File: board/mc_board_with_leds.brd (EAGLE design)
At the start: 131 x 76.6 mm, 30 parts, among them IC2 MEGA8-P, Q2 16MHz

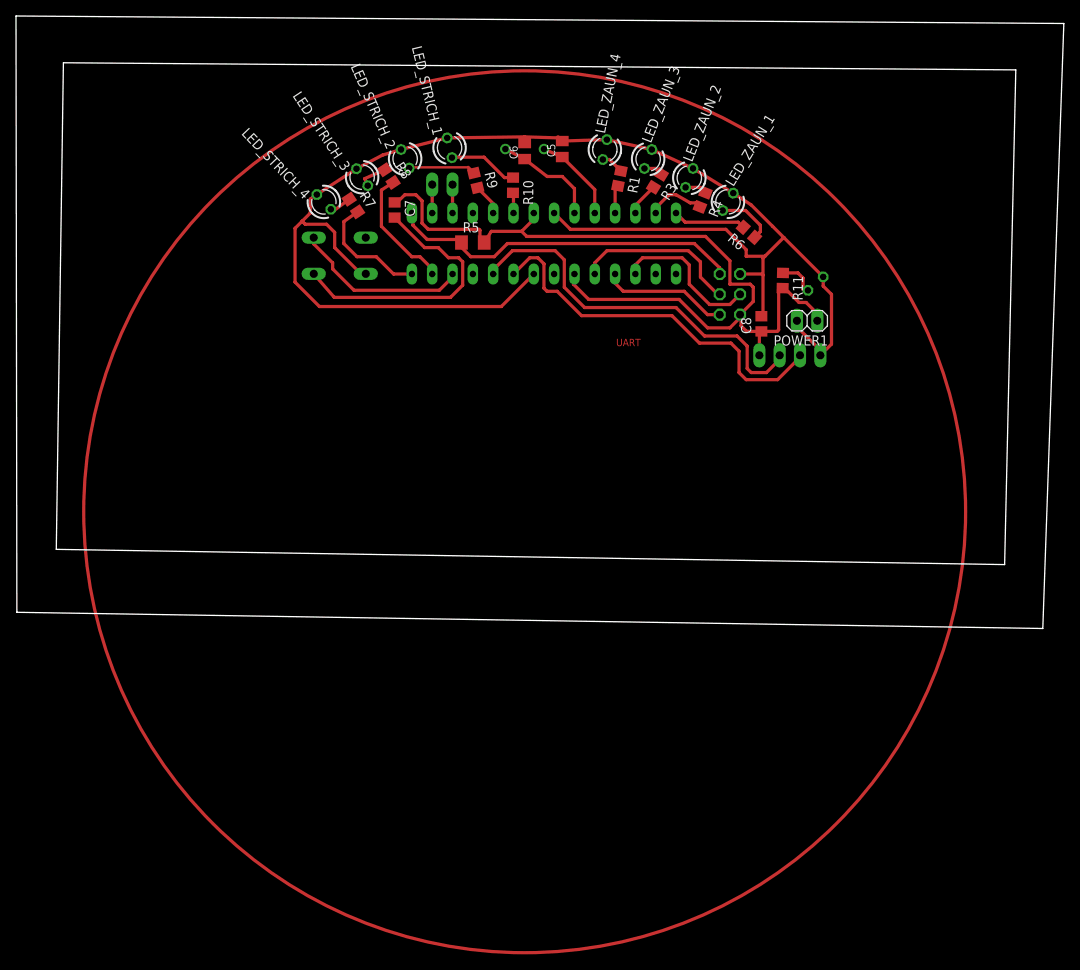
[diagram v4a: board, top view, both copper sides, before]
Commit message: added step up converter to schematic
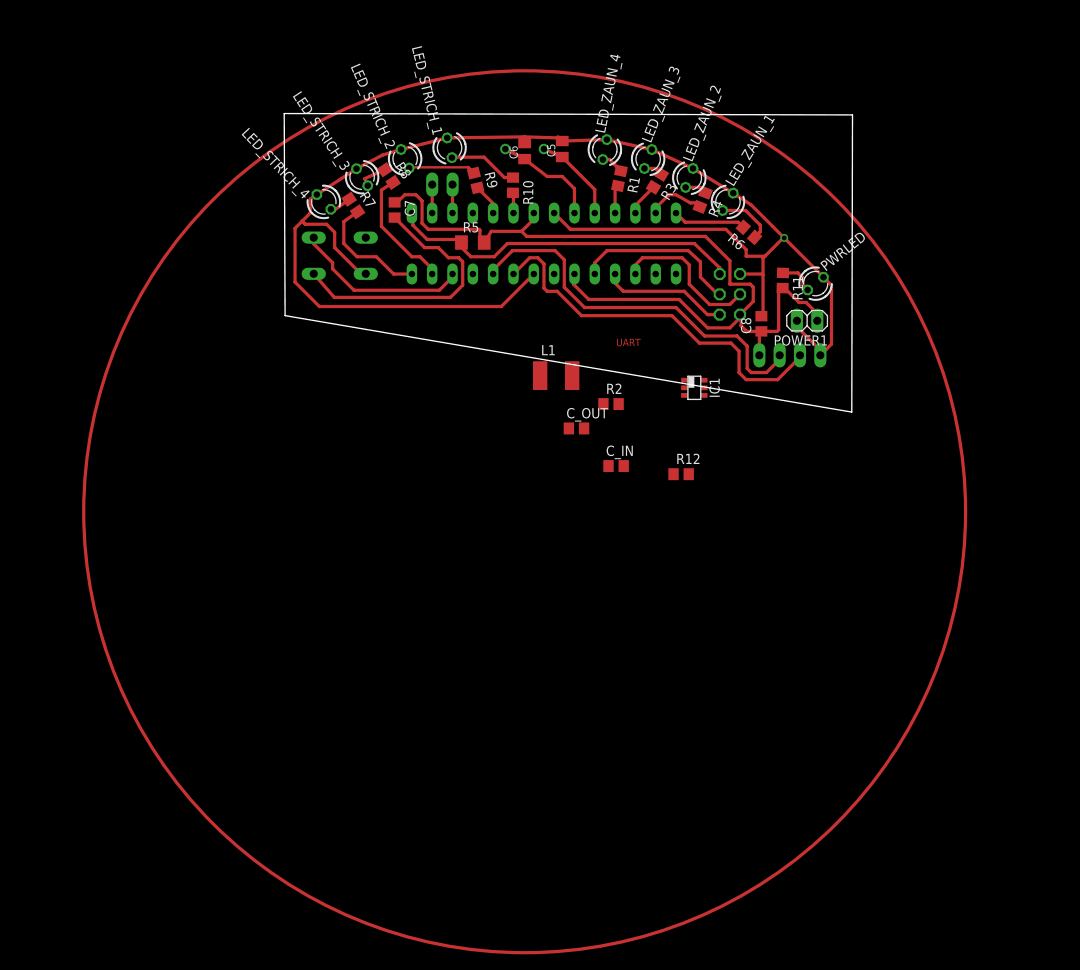
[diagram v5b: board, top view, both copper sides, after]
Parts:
- added C_IN, C_OUT: (no value), rcl-2:C0805
- added IC1: TPS61070DDC, texas:TSOT23-6_DDC
- added L1: (no value), rcl:L4532P
- added R12, R2: (no value), resistor:R0805
- flipped PWRLED to the top, turned to 38.6 degrees
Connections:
- new net N$5: IC1.1, L1.2
- new net N$6: IC1.4, R12.1, R2.2
- new net V_IN: C_IN.1, IC1.3, IC1.6, L1.1, POWER1.1
- net +5V: now also C_OUT.1, IC1.5, R2.1; no longer POWER1.1
- net GND: now also C_IN.2, C_OUT.2, IC1.2, R12.2
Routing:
- net +5V: track 109.2 -> 108.3 mm
- net GND: vias 0 -> 1
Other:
- board size 131 x 76.6 mm -> 71 x 37.3 mm
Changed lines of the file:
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@@
 <layer number="220" name="220bmp" color="21" fill="1" visible="no" active="no"/>
 <layer number="221" name="221bmp" color="22" fill="1" visible="no" active="no"/>
-<layer number="222" name="222bmp" color="23" fill="1" visible="no" active="no"/>
+<layer number="222" name="imagesize" color="23" fill="1" visible="yes" active="yes"/>
 <layer number="223" name="223bmp" color="24" fill="1" visible="no" active="no"/>
 <layer number="224" name="224bmp" color="25" fill="1" visible="no" active="no"/>
@@
 <board>
 <plain>
-<wire x1="-3.302" y1="-4.699" x2="115.24" y2="-6.604" width="0" layer="20"/>
-<wire x1="115.24" y1="-6.604" x2="116.637" y2="55.235" width="0" layer="20"/>
-<wire x1="116.637" y1="55.235" x2="-2.413" y2="56.124" width="0" layer="20"/>
-<wire x1="-2.413" y1="56.124" x2="-3.302" y2="-4.699" width="0" layer="20"/>
 <text x="66.675" y="20.701" size="0.9144" layer="1" font="vector" ratio="28">UART</text>
-<wire x1="-8.229528125" y1="-12.56735625" x2="-8.338403125" y2="61.970115625" width="0" layer="20"/>
-<wire x1="-8.338403125" y1="61.970115625" x2="122.64075" y2="61.033575" width="0" layer="20"/>
-<wire x1="122.64075" y1="61.033575" x2="120.011409375" y2="-14.59155" width="0" layer="20"/>
-<wire x1="120.011409375" y1="-14.59155" x2="-8.229528125" y2="-12.56735625" width="0" layer="20"/>
+<wire x1="25.298471875" y1="24.51664375" x2="25.189596875" y2="49.778115625" width="0" layer="20"/>
+<wire x1="25.189596875" y1="49.778115625" x2="96.22475" y2="49.603575" width="0" layer="20"/>
+<wire x1="96.22475" y1="49.603575" x2="96.135409375" y2="12.45945" width="0" layer="20"/>
+<wire x1="96.135409375" y1="12.45945" x2="25.298471875" y2="24.51664375" width="0" layer="20"/>
 <circle x="55.245" y="0" radius="55.118" width="0.4064" layer="1"/>
 </plain>
@@
 <element name="R10" library="resistor" package="R0805" value="470" x="53.788540625" y="40.819409375" rot="R269.6"/>
 <element name="R11" library="resistor" package="R0805" value="470" x="87.511846875" y="28.906165625" rot="R268.6"/>
-<element name="PWRLED" library="led" package="LED3MM" value="" x="91.60673125" y="28.5177875" rot="MR138.6"/>
+<element name="PWRLED" library="led" package="LED3MM" value="" x="91.60673125" y="28.5177875" rot="R38.6"/>
 <element name="Q2" library="crystal" package="HC49/S" value="16MHz" x="55.245" y="45.339" rot="MR0">
 <attribute name="MPN" value="" x="65.913" y="71.755" size="1.778" layer="28" rot="MR0" display="off"/>
@@
 <element name="HX1" library="pinhead" package="1X04" value="JP1" x="88.392" y="19.558" rot="MR0"/>
 <element name="UART1" library="pinhead" package="1X02" value="JP2" x="44.958" y="40.894" rot="MR180"/>
+<element name="IC1" library="texas" package="TSOT23-6_DDC" value="TPS61070DDC" x="76.454" y="15.494" rot="R270">
+<attribute name="MPN" value="TPS61070DDCR" x="76.454" y="15.494" size="1.778" layer="27" rot="R270" display="off"/>
+<attribute name="OC_NEWARK" value="64M3125" x="76.454" y="15.494" size="1.778" layer="27" rot="R270" display="off"/>
+<attribute name="MF" value="" x="76.454" y="15.494" size="1.778" layer="27" rot="R270" display="off"/>
+<attribute name="OC_FARNELL" value="1461062" x="76.454" y="15.494" size="1.778" layer="27" rot="R270" display="off"/>
+</element>
+<element name="L1" library="rcl" package="L4532P" value="" x="59.182" y="17.018"/>
+<element name="R2" library="resistor" package="R0805" value="" x="66.04" y="13.462"/>
+<element name="R12" library="resistor" package="R0805" value="" x="74.803" y="4.699"/>
+<element name="C_IN" library="rcl-2" package="C0805" value="" x="66.675" y="5.715"/>
+<element name="C_OUT" library="rcl-2" package="C0805" value="" x="61.722" y="10.414"/>
 </elements>
 <signals>
@@
 <wire x1="80.391" y1="35.306" x2="60.96" y2="35.306" width="0.4064" layer="1"/>
 <wire x1="60.96" y1="35.306" x2="58.928" y2="37.338" width="0.4064" layer="1"/>
-<wire x1="92.559375" y1="29.357653125" x2="87.693203125" y2="34.2261125" width="0.4064" layer="1"/>
 <wire x1="87.693203125" y1="34.2261125" x2="86.233" y2="35.687" width="0.4064" layer="1"/>
 <wire x1="81.31878125" y1="39.828921875" x2="83.566" y2="38.354" width="0.4064" layer="1"/>
@@
 <wire x1="87.5661125" y1="34.2261125" x2="87.693203125" y2="34.2261125" width="0.4064" layer="1"/>
 <wire x1="92.202" y1="19.558" x2="93.599" y2="20.955" width="0.4064" layer="1"/>
-<wire x1="93.599" y1="20.955" x2="93.599" y2="27.178" width="0.4064" layer="1"/>
-<wire x1="93.599" y1="27.178" x2="92.559375" y2="28.217625" width="0.4064" layer="1"/>
-<wire x1="92.559375" y1="28.217625" x2="92.559375" y2="29.357653125" width="0.4064" layer="1"/>
+<wire x1="93.599" y1="20.955" x2="93.599" y2="28.310371875" width="0.4064" layer="1"/>
 <wire x1="89.281" y1="23.876" x2="89.281" y2="23.114" width="0.4064" layer="1"/>
 <wire x1="89.281" y1="23.114" x2="92.202" y2="20.193" width="0.4064" layer="1"/>
@@
 <wire x1="55.245" y1="46.863" x2="45.55835" y2="46.732621875" width="0.4064" layer="1"/>
 <wire x1="55.245" y1="46.863" x2="59.555" y2="46.728" width="0.4064" layer="1"/>
+<via x="87.693203125" y="34.2261125" extent="1-16" drill="0.6" shape="square"/>
+<wire x1="93.599" y1="28.310371875" x2="92.599259375" y2="29.3101125" width="0.4064" layer="1"/>
+<wire x1="92.599259375" y1="29.3101125" x2="92.599259375" y2="29.32005625" width="0.4064" layer="1"/>
+<wire x1="92.599259375" y1="29.32005625" x2="87.693203125" y2="34.2261125" width="0.4064" layer="1"/>
+<contactref element="IC1" pad="2"/>
+<contactref element="C_IN" pad="2"/>
+<contactref element="C_OUT" pad="2"/>
+<contactref element="R12" pad="2"/>
+<wire x1="67.625" y1="5.715" x2="62.672" y2="10.414" width="0" layer="19" extent="1-1"/>
+<wire x1="75.753" y1="4.699" x2="67.625" y2="5.715" width="0" layer="19" extent="1-1"/>
+<wire x1="75.204" y1="15.494" x2="75.753" y2="4.699" width="0" layer="19" extent="1-1"/>
+<wire x1="29.591" y1="25.654" x2="75.204" y2="15.494" width="0" layer="19" extent="1-1"/>
 </signal>
 <signal name="+5V">
@@
 <contactref element="C7" pad="1"/>
 <contactref element="ISP1" pad="2"/>
-<contactref element="POWER1" pad="1"/>
 <contactref element="HX1" pad="4"/>
 <wire x1="84.836" y1="22.545" x2="84.582" y2="22.291" width="0.4064" layer="1"/>
@@
 <wire x1="83.82" y1="28.067" x2="83.82" y2="26.289" width="0.4064" layer="1"/>
 <wire x1="83.82" y1="26.289" x2="82.169" y2="24.638" width="0.4064" layer="1"/>
-<wire x1="91.821" y1="23.876" x2="91.821" y2="24.765" width="0.4064" layer="1"/>
 <wire x1="91.821" y1="24.765" x2="90.424" y2="26.162" width="0.4064" layer="1"/>
 <wire x1="90.424" y1="26.162" x2="89.535" y2="26.162" width="0.4064" layer="1"/>
@@
 <wire x1="40.259" y1="39.624" x2="39.304" y2="38.669" width="0.4064" layer="1"/>
 <wire x1="39.304" y1="38.669" x2="38.989" y2="38.669" width="0.4064" layer="1"/>
+<contactref element="IC1" pad="5"/>
+<contactref element="R2" pad="1"/>
+<contactref element="C_OUT" pad="1"/>
+<wire x1="65.09" y1="13.462" x2="60.772" y2="10.414" width="0" layer="19" extent="1-1"/>
+<wire x1="77.704" y1="15.494" x2="65.09" y2="13.462" width="0" layer="19" extent="1-1"/>
+<wire x1="43.18" y1="35.306" x2="77.704" y2="15.494" width="0" layer="19" extent="1-1"/>
 </signal>
 <signal name="PB4/MISO">
@@
 <wire x1="87.53505625" y1="29.85588125" x2="89.39711875" y2="29.85588125" width="0.4064" layer="1"/>
 <wire x1="89.39711875" y1="29.85588125" x2="90.043" y2="29.21" width="0.4064" layer="1"/>
-<wire x1="90.043" y1="29.21" x2="90.043" y2="27.800684375" width="0.4064" layer="1"/>
-<wire x1="90.043" y1="27.800684375" x2="90.654090625" y2="27.67791875" width="0.4064" layer="1"/>
+<wire x1="90.043" y1="29.21" x2="90.043" y2="28.296659375" width="0.4064" layer="1"/>
+<wire x1="90.043" y1="28.296659375" x2="90.6142" y2="27.725459375" width="0.4064" layer="1"/>
 </signal>
 <signal name="N$4">
@@
 <wire x1="76.649509375" y1="38.608" x2="77.1496625" y2="38.107846875" width="0.4064" layer="1"/>
 </signal>
+<signal name="V_IN">
+<contactref element="POWER1" pad="1"/>
+<contactref element="IC1" pad="6"/>
+<contactref element="C_IN" pad="1"/>
+<contactref element="L1" pad="1"/>
+<contactref element="IC1" pad="3"/>
+<wire x1="77.704" y1="16.444" x2="91.821" y2="23.876" width="0" layer="19" extent="1-1"/>
+<wire x1="75.204" y1="14.544" x2="77.704" y2="16.444" width="0" layer="19" extent="1-1"/>
+<wire x1="57.182" y1="17.018" x2="77.704" y2="16.444" width="0" layer="19" extent="1-1"/>
+<wire x1="65.725" y1="5.715" x2="57.182" y2="17.018" width="0" layer="19" extent="1-1"/>
+</signal>
+<signal name="N$5">
+<contactref element="IC1" pad="1"/>
+<contactref element="L1" pad="2"/>
+<wire x1="61.182" y1="17.018" x2="75.204" y2="16.444" width="0" layer="19" extent="1-1"/>
+</signal>
+<signal name="N$6">
+<contactref element="R12" pad="1"/>
+<contactref element="R2" pad="2"/>
+<contactref element="IC1" pad="4"/>
+<wire x1="66.99" y1="13.462" x2="73.853" y2="4.699" width="0" layer="19" extent="1-1"/>
+<wire x1="77.704" y1="14.544" x2="66.99" y2="13.462" width="0" layer="19" extent="1-1"/>
+</signal>
 </signals>

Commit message: led board and case now match exactly
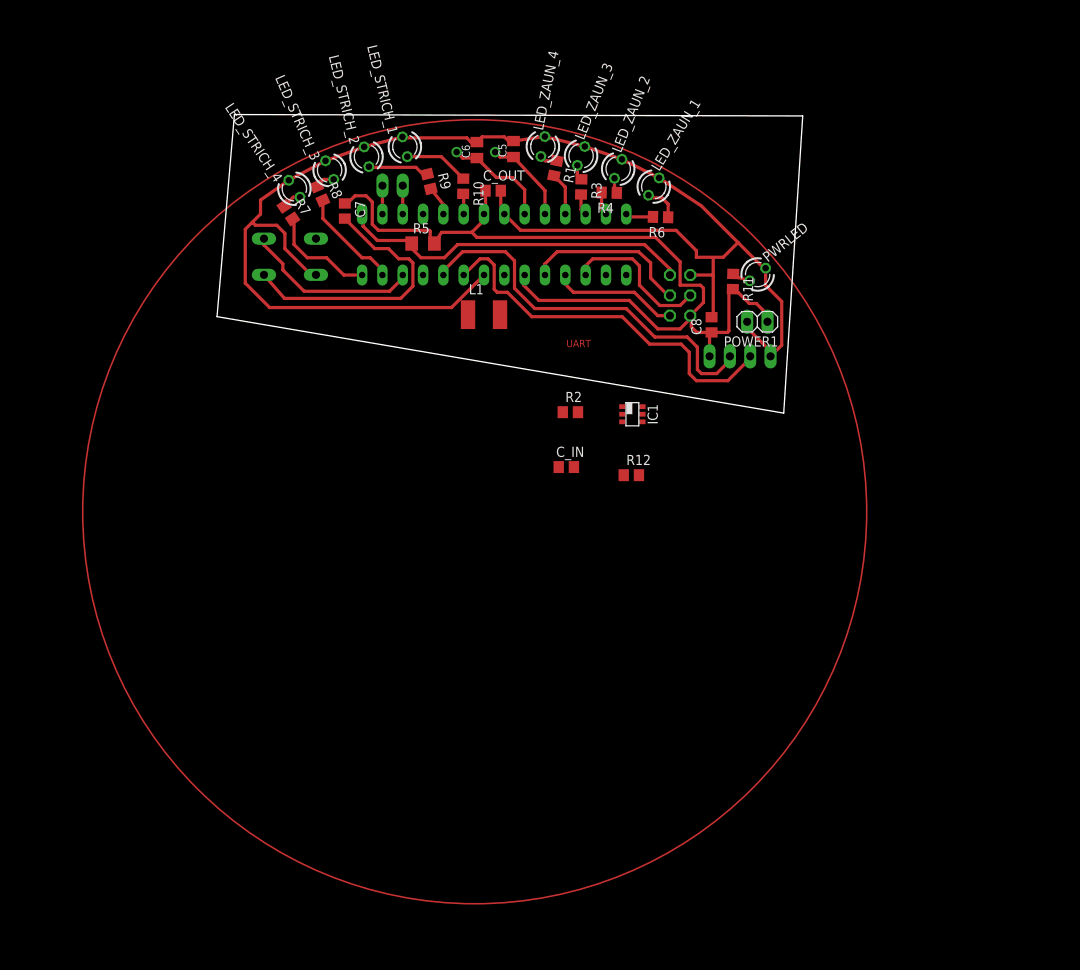
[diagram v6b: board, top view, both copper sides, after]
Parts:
- moved C_OUT 31.5 mm to (51.3, 40.1)
- moved L1 11.8 mm to (50.2, 24.6)
- moved R4 11.7 mm to (65.8, 39.9), turned to 178.6 degrees
- moved R6 11.2 mm to (72.2, 36.8), turned to 178.6 degrees
- moved R3 9.56 mm to (62.3, 40.6), turned to 268.6 degrees
- moved LED_ZAUN_1 9.46 mm to (71.4, 40.6)
- moved LED_ZAUN_2 8.96 mm to (66.9, 42.9)
- moved R8 8.90 mm to (29.6, 39.8), turned to 293.6 degrees
- moved IC1 8.42 mm to (68.7, 12.2)
- moved LED_ZAUN_3 8.39 mm to (62.3, 44.5)
- moved R7 8.18 mm to (25.7, 37.4)
- moved R1 8.10 mm to (59.1, 42.9)
- moved LED_ZAUN_4 7.76 mm to (57.5, 45.7)
- moved PWRLED 7.33 mm to (84.4, 29.7)
- moved R10 6.22 mm to (47.6, 40.7)
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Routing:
- net PB0/LED_ZAUN_1: track 9.14 -> 3.48 mm
- net PD7/LED_ZAUN_2: track 7.32 -> 2.92 mm
- net +5V: track 108.3 -> 111.3 mm
- net GND: track 188.4 -> 191.2 mm, vias 1 -> 0
- net N$7: track 7.29 -> 4.56 mm
- net PC4/LED_STRICH_3: track 15.5 -> 13.0 mm
- net N$13: track 4.50 -> 2.28 mm
- net PC5/LED_STRICH_4: track 14.9 -> 12.8 mm
- net PD5/LED_ZAUN_4: track 3.75 -> 5.39 mm
- net PD6/LED_ZAUN_3: track 4.16 -> 2.68 mm
- net N$10: track 3.70 -> 2.47 mm
- net N$11: track 8.52 -> 7.67 mm
- net N$3: track 2.76 -> 1.95 mm
- net N$1: track 2.85 -> 2.23 mm
- net N$12: track 8.72 -> 8.14 mm
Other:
- board size 71 x 37.3 mm -> 73.2 x 37.3 mm

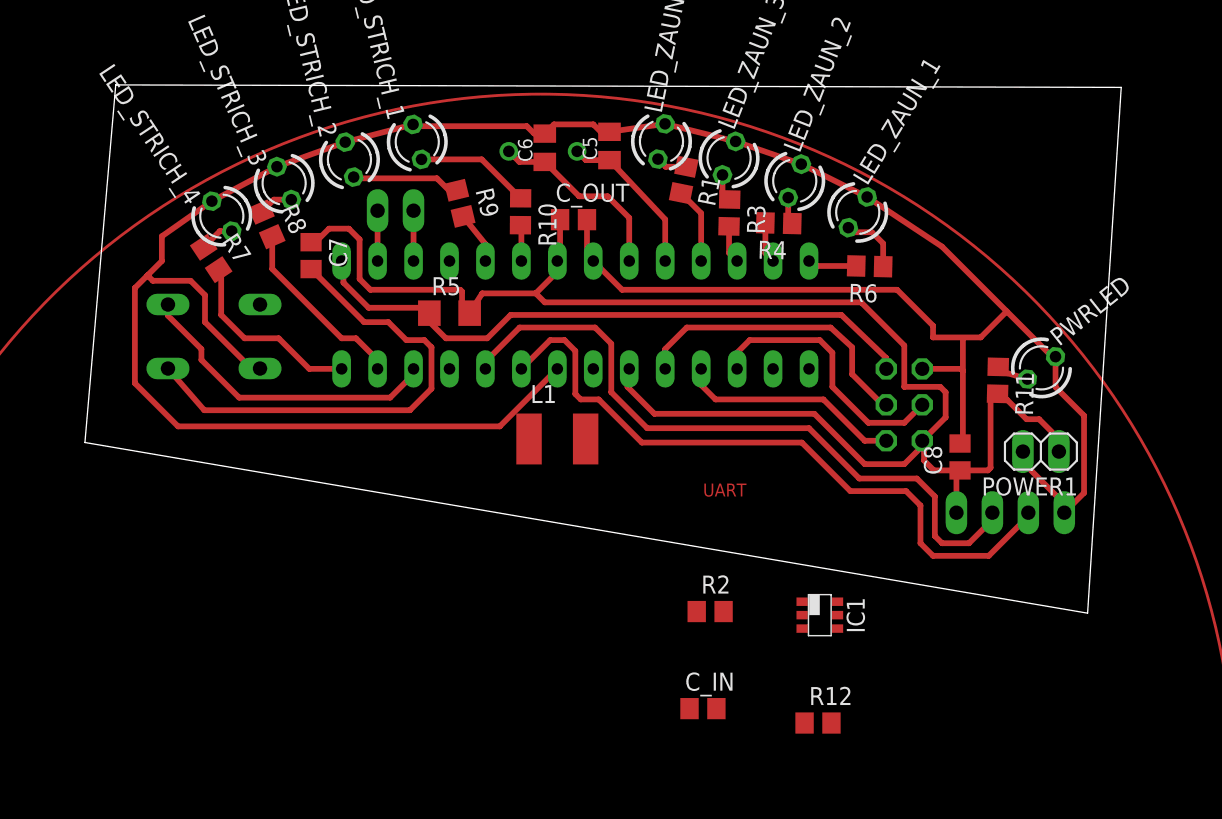
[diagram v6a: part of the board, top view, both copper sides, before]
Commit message: integrated pull up into board layout
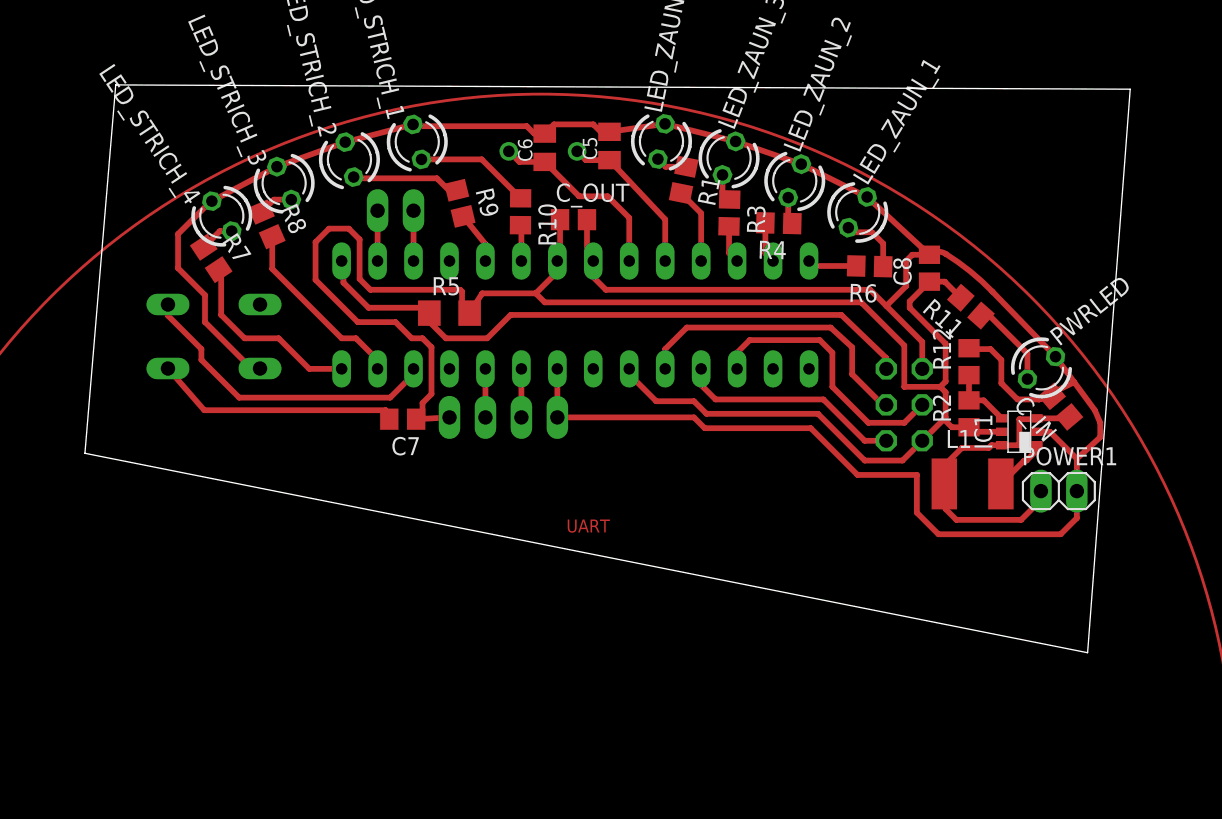
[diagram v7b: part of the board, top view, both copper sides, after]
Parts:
- moved HX1 36.4 mm to (46.4, 26.2)
- moved C_IN 33.1 mm to (85.7, 26.9), turned to 130 degrees
- moved L1 29.5 mm to (79.5, 21.5)
- moved R12 27.7 mm to (79.2, 30.1), turned to 90 degrees
- moved R2 23.0 mm to (79.2, 26.4), turned to 90 degrees
- moved IC1 19.1 mm to (82.8, 25.1), turned to 90 degrees
- moved C8 13.5 mm to (76.5, 36.7)
- moved C7 13.2 mm to (39.2, 26.0), turned to 180 degrees
- moved R11 5.54 mm to (79.4, 34.0), turned to 138.6 degrees
- moved POWER1 3.07 mm to (85.6, 21.0), turned to 0 degrees
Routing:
- net PC1/SCK: track 48.5 -> 3.43 mm
- net PC0/DT: track 47.7 -> 3.43 mm
- net V_IN: track 0.00 -> 23.0 mm
- net N$15: track 34.3 -> 17.4 mm
- net +5V: track 111.3 -> 126.5 mm
- net N$6: track 0.00 -> 4.62 mm
- net N$13: track 2.28 -> 6.19 mm
- net N$5: track 0.00 -> 3.90 mm
- net GND: track 191.2 -> 192.8 mm
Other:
- board size 73.2 x 37.3 mm -> 73.8 x 40.1 mm
